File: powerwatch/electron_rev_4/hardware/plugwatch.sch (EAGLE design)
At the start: 122 parts, among them J1 DM3AT-SF-PEJM5, Q1 SI223DDS, U1 BGA725L6-ALT, U10 SIP32510, U12 SIP32510, U13 AB1815-T3, U16 MAX6746, U2 SAFFB1G56KB0F0A, U3 IRM-03-5V, U4 MAX-M8, U5 MAX9910, U6 LIS2DW12, U8 MAX9910, U9 SIP32510, X1 ABS07-32.768KHZ-7-T

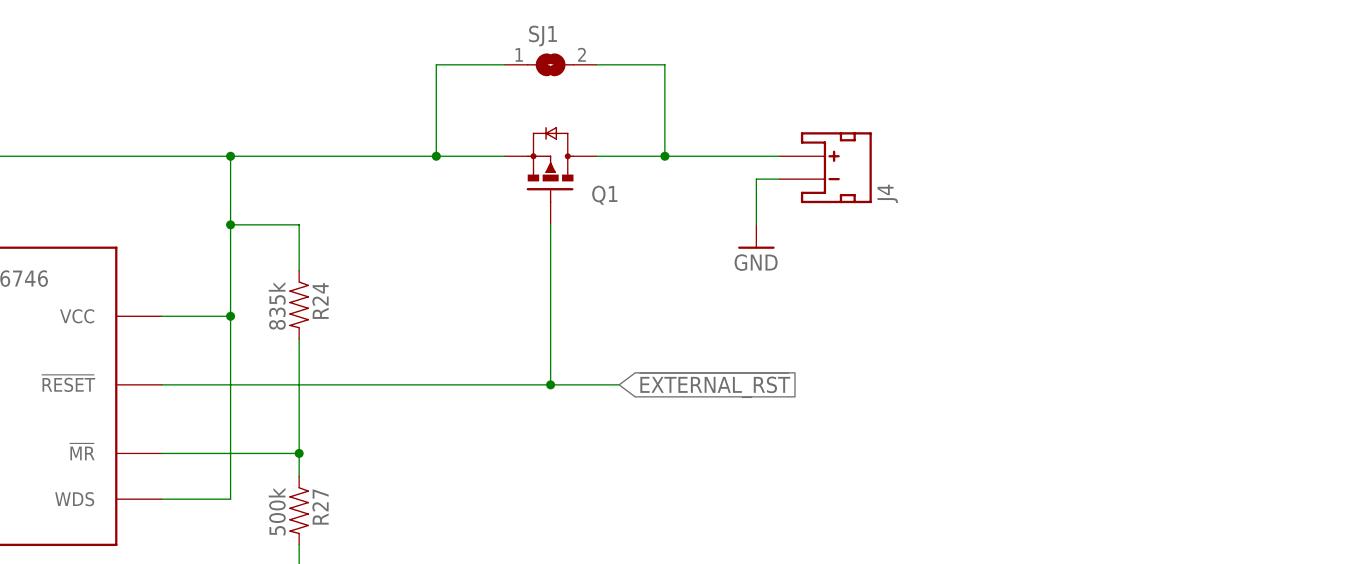
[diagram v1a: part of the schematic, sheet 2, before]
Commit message: add inverter to watchdog reset line
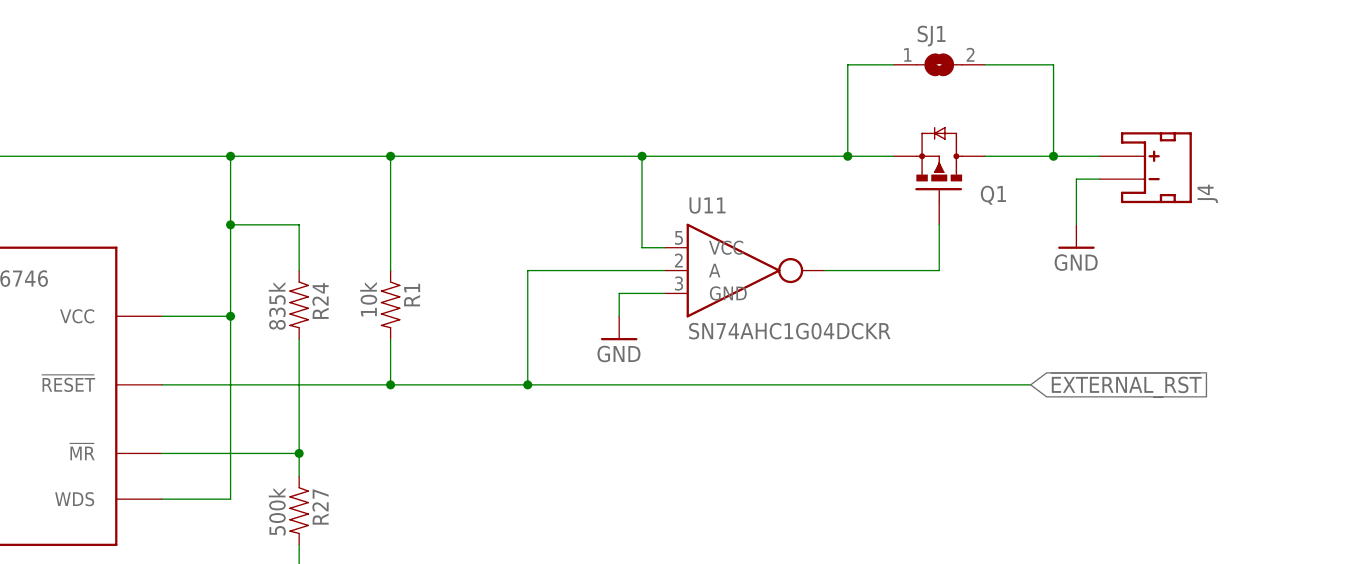
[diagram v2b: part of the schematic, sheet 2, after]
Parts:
- added R1: 10k, passives:RESISTOR0402_RES
- added U11: SN74AHC1G04DCKR, chips:SN74AUP1T14DCKR
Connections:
- new net N$9: Q1.G, U11.Y
- net !EXTERNAL_RST: now also R1.2, U11.A; no longer Q1.G
- net GND: now also U11.GND
- net N$23: now also R1.1, U11.VCC
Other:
- moved on the sheet: J4, Q1, SJ1
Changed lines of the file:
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@@
 <part name="TP16" library="headers" deviceset="TEST_POINT_0.040IN" device=""/>
 <part name="TP17" library="headers" deviceset="TEST_POINT_0.040IN" device=""/>
+<part name="R1" library="passives" deviceset="RESISTOR" device="0402_RES" value="10k">
+<attribute name="DESCRIPTION" value="RES SMD 150 OHM 1% 1/16W 0402"/>
+<attribute name="DIGIKEY" value="RMCF0402FT150RCT-ND"/>
+<attribute name="MANUFACTURER" value="Stackpole Electronics"/>
+<attribute name="MPN" value="RMCF0402FT150R"/>
+</part>
+<part name="U11" library="chips" deviceset="SN74AUP1T14DCKR" device="" value="SN74AHC1G04DCKR">
+<attribute name="DIGIKEY" value="296-1090-1-ND"/>
+</part>
+<part name="GND3" library="supply1" library_urn="urn:adsk.eagle:library:371" deviceset="GND" device=""/>
 </parts>
 <sheets>
@@
 drop doesn't work as expected
 with the charging circuit</text>
-<text x="203.2" y="175.26" size="1.778" layer="98" align="bottom-center">Use jumper cable from
+<text x="241.3" y="170.18" size="1.778" layer="98" align="bottom-center">Use jumper cable from
 board to particle</text>
 <text x="172.72" y="116.84" size="1.778" layer="98" align="bottom-center">Voltage supervisor.
@@
 <instance part="FRAME6" gate="G$2" x="152.4" y="0"/>
 <instance part="J3" gate="G$1" x="55.88" y="162.56" rot="R90"/>
-<instance part="J4" gate="G$1" x="198.12" y="162.56" rot="MR90"/>
+<instance part="J4" gate="G$1" x="233.68" y="162.56" rot="MR90"/>
 <instance part="GND13" gate="1" x="66.04" y="154.94"/>
 <instance part="R24" gate="G$1" x="139.7" y="147.32" rot="R270">
@@
 <attribute name="DIGIKEY" x="139.7" y="124.46" size="1.27" layer="96" rot="R270" display="off"/>
 </instance>
-<instance part="Q1" gate="G$1" x="167.64" y="165.1" smashed="yes" rot="MR90">
-<attribute name="NAME" x="175.26" y="160.02" size="1.778" layer="95" rot="MR0"/>
-</instance>
-<instance part="GND39" gate="1" x="190.5" y="154.94"/>
-<instance part="SJ1" gate="1" x="167.64" y="175.26"/>
+<instance part="Q1" gate="G$1" x="210.82" y="165.1" smashed="yes" rot="MR90">
+<attribute name="NAME" x="218.44" y="160.02" size="1.778" layer="95" rot="MR0"/>
+</instance>
+<instance part="GND39" gate="1" x="226.06" y="154.94"/>
+<instance part="SJ1" gate="1" x="210.82" y="175.26"/>
 <instance part="U16" gate="G$1" x="106.68" y="139.7"/>
 <instance part="GND42" gate="1" x="86.36" y="116.84"/>
@@
 <attribute name="DIGIKEY" x="101.6" y="53.34" size="1.27" layer="96" rot="R270" display="off"/>
 </instance>
+<instance part="R1" gate="G$1" x="149.86" y="147.32" rot="R270">
+<attribute name="DIGIKEY" x="149.86" y="147.32" size="1.27" layer="96" rot="R270" display="off"/>
+</instance>
+<instance part="U11" gate="G$1" x="185.42" y="152.4"/>
+<instance part="GND3" gate="1" x="175.26" y="144.78"/>
 </instances>
 <busses>
@@
 <segment>
 <pinref part="J4" gate="G$1" pin="-"/>
-<wire x1="193.04" y1="162.56" x2="190.5" y2="162.56" width="0.1524" layer="91"/>
+<wire x1="228.6" y1="162.56" x2="226.06" y2="162.56" width="0.1524" layer="91"/>
 <pinref part="GND39" gate="1" pin="GND"/>
-<wire x1="190.5" y1="162.56" x2="190.5" y2="157.48" width="0.1524" layer="91"/>
+<wire x1="226.06" y1="162.56" x2="226.06" y2="157.48" width="0.1524" layer="91"/>
 </segment>
 <segment>
@@
 <junction x="160.02" y="40.64"/>
 </segment>
+<segment>
+<pinref part="U11" gate="G$1" pin="GND"/>
+<wire x1="180.34" y1="149.86" x2="175.26" y2="149.86" width="0.1524" layer="91"/>
+<pinref part="GND3" gate="1" pin="GND"/>
+<wire x1="175.26" y1="149.86" x2="175.26" y2="147.32" width="0.1524" layer="91"/>
+</segment>
 </net>
 <net name="N$23" class="0">
@@
 <pinref part="Q1" gate="G$1" pin="S"/>
 <wire x1="60.96" y1="165.1" x2="132.08" y2="165.1" width="0.1524" layer="91"/>
-<wire x1="132.08" y1="165.1" x2="154.94" y2="165.1" width="0.1524" layer="91"/>
-<wire x1="154.94" y1="165.1" x2="162.56" y2="165.1" width="0.1524" layer="91"/>
-<wire x1="154.94" y1="165.1" x2="154.94" y2="175.26" width="0.1524" layer="91"/>
-<junction x="154.94" y="165.1"/>
+<wire x1="132.08" y1="165.1" x2="149.86" y2="165.1" width="0.1524" layer="91"/>
+<wire x1="149.86" y1="165.1" x2="177.8" y2="165.1" width="0.1524" layer="91"/>
+<wire x1="177.8" y1="165.1" x2="200.66" y2="165.1" width="0.1524" layer="91"/>
+<wire x1="200.66" y1="165.1" x2="205.74" y2="165.1" width="0.1524" layer="91"/>
+<wire x1="200.66" y1="165.1" x2="200.66" y2="175.26" width="0.1524" layer="91"/>
+<junction x="200.66" y="165.1"/>
 <pinref part="SJ1" gate="1" pin="1"/>
-<wire x1="154.94" y1="175.26" x2="162.56" y2="175.26" width="0.1524" layer="91"/>
+<wire x1="200.66" y1="175.26" x2="205.74" y2="175.26" width="0.1524" layer="91"/>
 <pinref part="U16" gate="G$1" pin="VCC"/>
 <wire x1="124.46" y1="147.32" x2="132.08" y2="147.32" width="0.1524" layer="91"/>
@@
 <wire x1="132.08" y1="127" x2="132.08" y2="147.32" width="0.1524" layer="91"/>
 <junction x="132.08" y="147.32"/>
+<pinref part="R1" gate="G$1" pin="1"/>
+<wire x1="149.86" y1="152.4" x2="149.86" y2="165.1" width="0.1524" layer="91"/>
+<junction x="149.86" y="165.1"/>
+<pinref part="U11" gate="G$1" pin="VCC"/>
+<wire x1="180.34" y1="154.94" x2="177.8" y2="154.94" width="0.1524" layer="91"/>
+<wire x1="177.8" y1="154.94" x2="177.8" y2="165.1" width="0.1524" layer="91"/>
+<junction x="177.8" y="165.1"/>
 </segment>
 </net>
 <net name="!EXTERNAL_RST" class="0">
 <segment>
-<wire x1="124.46" y1="139.7" x2="167.64" y2="139.7" width="0.1524" layer="91"/>
-<pinref part="Q1" gate="G$1" pin="G"/>
-<wire x1="167.64" y1="139.7" x2="167.64" y2="157.48" width="0.1524" layer="91"/>
-<wire x1="167.64" y1="139.7" x2="175.26" y2="139.7" width="0.1524" layer="91"/>
-<junction x="167.64" y="139.7"/>
-<label x="175.26" y="139.7" size="1.778" layer="95" xref="yes"/>
+<wire x1="124.46" y1="139.7" x2="149.86" y2="139.7" width="0.1524" layer="91"/>
+<wire x1="149.86" y1="139.7" x2="165.1" y2="139.7" width="0.1524" layer="91"/>
+<label x="220.98" y="139.7" size="1.778" layer="95" xref="yes"/>
 <pinref part="U16" gate="G$1" pin="!RESET"/>
+<pinref part="R1" gate="G$1" pin="2"/>
+<wire x1="165.1" y1="139.7" x2="220.98" y2="139.7" width="0.1524" layer="91"/>
+<wire x1="149.86" y1="144.78" x2="149.86" y2="139.7" width="0.1524" layer="91"/>
+<junction x="149.86" y="139.7"/>
+<pinref part="U11" gate="G$1" pin="A"/>
+<wire x1="180.34" y1="152.4" x2="165.1" y2="152.4" width="0.1524" layer="91"/>
+<wire x1="165.1" y1="152.4" x2="165.1" y2="139.7" width="0.1524" layer="91"/>
+<junction x="165.1" y="139.7"/>
 </segment>
 </net>
@@
 <pinref part="Q1" gate="G$1" pin="D"/>
 <pinref part="J4" gate="G$1" pin="+"/>
-<wire x1="172.72" y1="165.1" x2="180.34" y2="165.1" width="0.1524" layer="91"/>
+<wire x1="215.9" y1="165.1" x2="223.52" y2="165.1" width="0.1524" layer="91"/>
 <pinref part="SJ1" gate="1" pin="2"/>
-<wire x1="180.34" y1="165.1" x2="193.04" y2="165.1" width="0.1524" layer="91"/>
-<wire x1="172.72" y1="175.26" x2="180.34" y2="175.26" width="0.1524" layer="91"/>
-<wire x1="180.34" y1="175.26" x2="180.34" y2="165.1" width="0.1524" layer="91"/>
-<junction x="180.34" y="165.1"/>
+<wire x1="223.52" y1="165.1" x2="228.6" y2="165.1" width="0.1524" layer="91"/>
+<wire x1="215.9" y1="175.26" x2="223.52" y2="175.26" width="0.1524" layer="91"/>
+<wire x1="223.52" y1="175.26" x2="223.52" y2="165.1" width="0.1524" layer="91"/>
+<junction x="223.52" y="165.1"/>
 </segment>
 </net>
@@
 </segment>
 </net>
+<net name="N$9" class="0">
+<segment>
+<pinref part="U11" gate="G$1" pin="Y"/>
+<wire x1="198.12" y1="152.4" x2="210.82" y2="152.4" width="0.1524" layer="91"/>
+<pinref part="Q1" gate="G$1" pin="G"/>
+<wire x1="210.82" y1="152.4" x2="210.82" y2="157.48" width="0.1524" layer="91"/>
+</segment>
+</net>

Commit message: doing routing
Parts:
- removed Q1: SI223DDS, fets:SI223DDS
- removed R20: 10k, passives:RESISTOR0402_RES
- removed SJ1: (no value), jumper:SJW
- removed U11: SN74AHC1G04DCKR, chips:SN74AUP1T14DCKR
- added C4: 1uF, passives:CAPACITOR0402_CAP
- C1, C24, C29, C3: device passives:CAPACITOR0603_CAP -> passives:CAPACITOR0402_CAP
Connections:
- removed net !RTC_INT2: R20.2, U13.!IRQ2
- removed net N$35: J4.+, Q1.D, SJ1.2
- removed net N$9: Q1.G, U11.Y
- net !EXTERNAL_RST: no longer U11.A
- net GND: now also C4.2; no longer U11.GND
- net N$23: now also J4.+; no longer Q1.S, SJ1.1, U11.VCC
- net VCC: now also C4.1; no longer R20.1
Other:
- note added: "No need to pull up to VBAT. If we don't have VCC the particle won't be on anyways."
- note added: "Watchdog Timeout = 297s Reset Period = ~4s"
- note added: "We want to capture power on/off events on EXTI - use a resistor devider to get the right voltage."
- note removed: "If we dont' have VCC, nothing will be able to read these anyways."
